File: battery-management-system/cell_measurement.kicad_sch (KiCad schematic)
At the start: 26 parts, among them Q5 DMN3730U, Q6 BS250FTA, Q7 BS250FTA, Q8 BS250FTA, Q9 BS250FTA, U10 LM2904M8-13, U11 LM2904M8-13, U6 LM2904M8-13, U7 LM2904M8-13

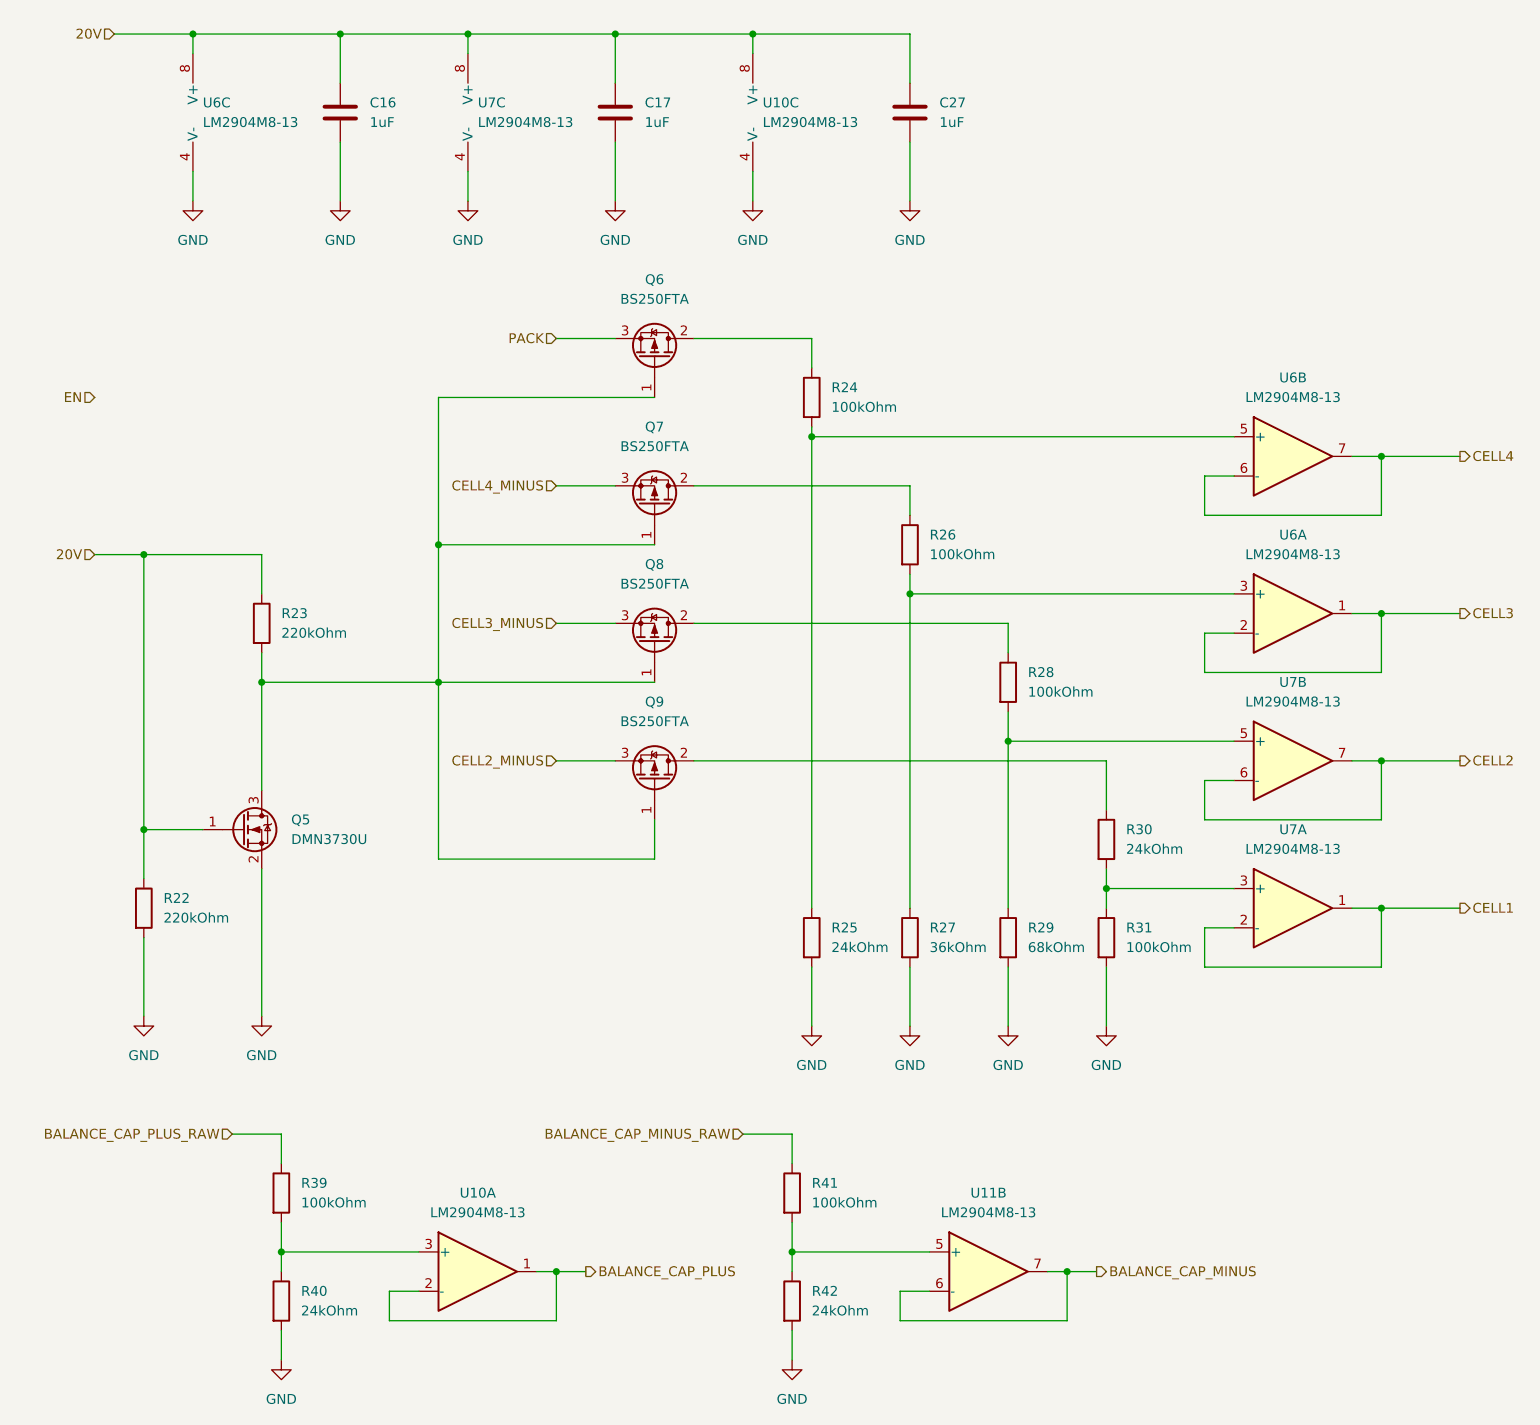
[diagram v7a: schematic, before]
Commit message: fix electrical rule checker errors
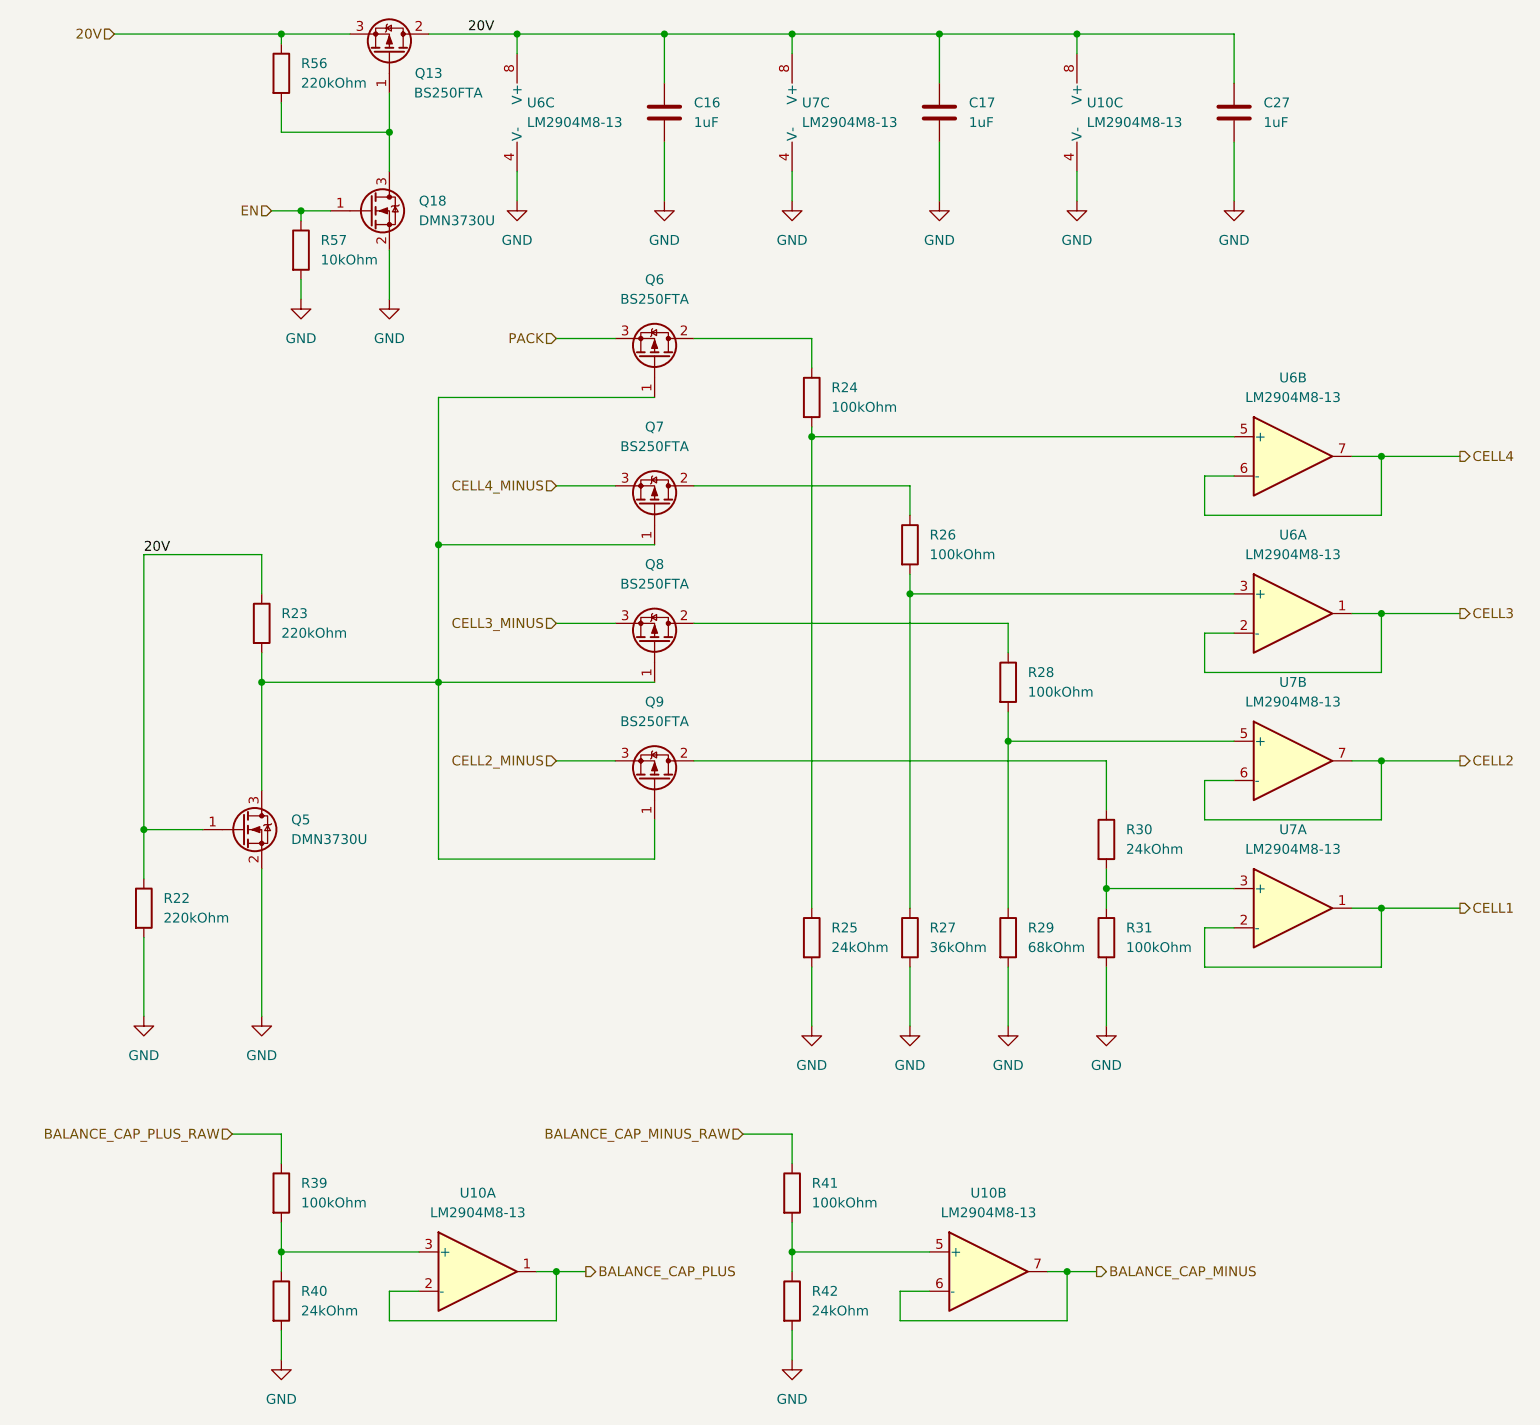
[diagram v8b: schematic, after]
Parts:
- added Q13: BS250FTA, benediktibk:SOT-23, symbol benediktibk:BS250FTA
- added Q18: DMN3730U, benediktibk:SOT-23, symbol benediktibk:DMN3730U
- added R56: 220kOhm, benediktibk:R_0603_1608Metric_Pad0.98x0.95mm_HandSolder, symbol benediktibk:R_220kOhm_SMD_0603_100mW_1%
- added R57: 10kOhm, benediktibk:R_0603_1608Metric_Pad0.98x0.95mm_HandSolder, symbol benediktibk:R_10kOhm_SMD_0603_100mW_1%
- renumbered U11 to U10
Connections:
- net 20V: now also Q13.2 (D), Q13.3 (S), R56.1
- net EN: now also Q18.1 (G), R57.1
- net GND: now also Q18.2 (S), R57.2
- new net: Q13.1 (G), Q18.3 (D), R56.2
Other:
- moved on the sheet: C16, C17, C27, U10C, U6C, U7C
